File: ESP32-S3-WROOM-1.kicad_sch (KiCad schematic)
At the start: 24 parts, among them J11 Conn_01x08, J13 Conn_02x09_Top_Bottom, J14 Conn_01x09, J15 Conn_02x09_Top_Bottom, J4 B4B-ZRLFSN, J6 Conn_01x09, J7 Conn_02x20_Counter_Clockwise, J8 Conn_01x08, J9 Conn_01x08, SW4 SW_Push, U8 ESP32-S3-WROOM-1-N8R2

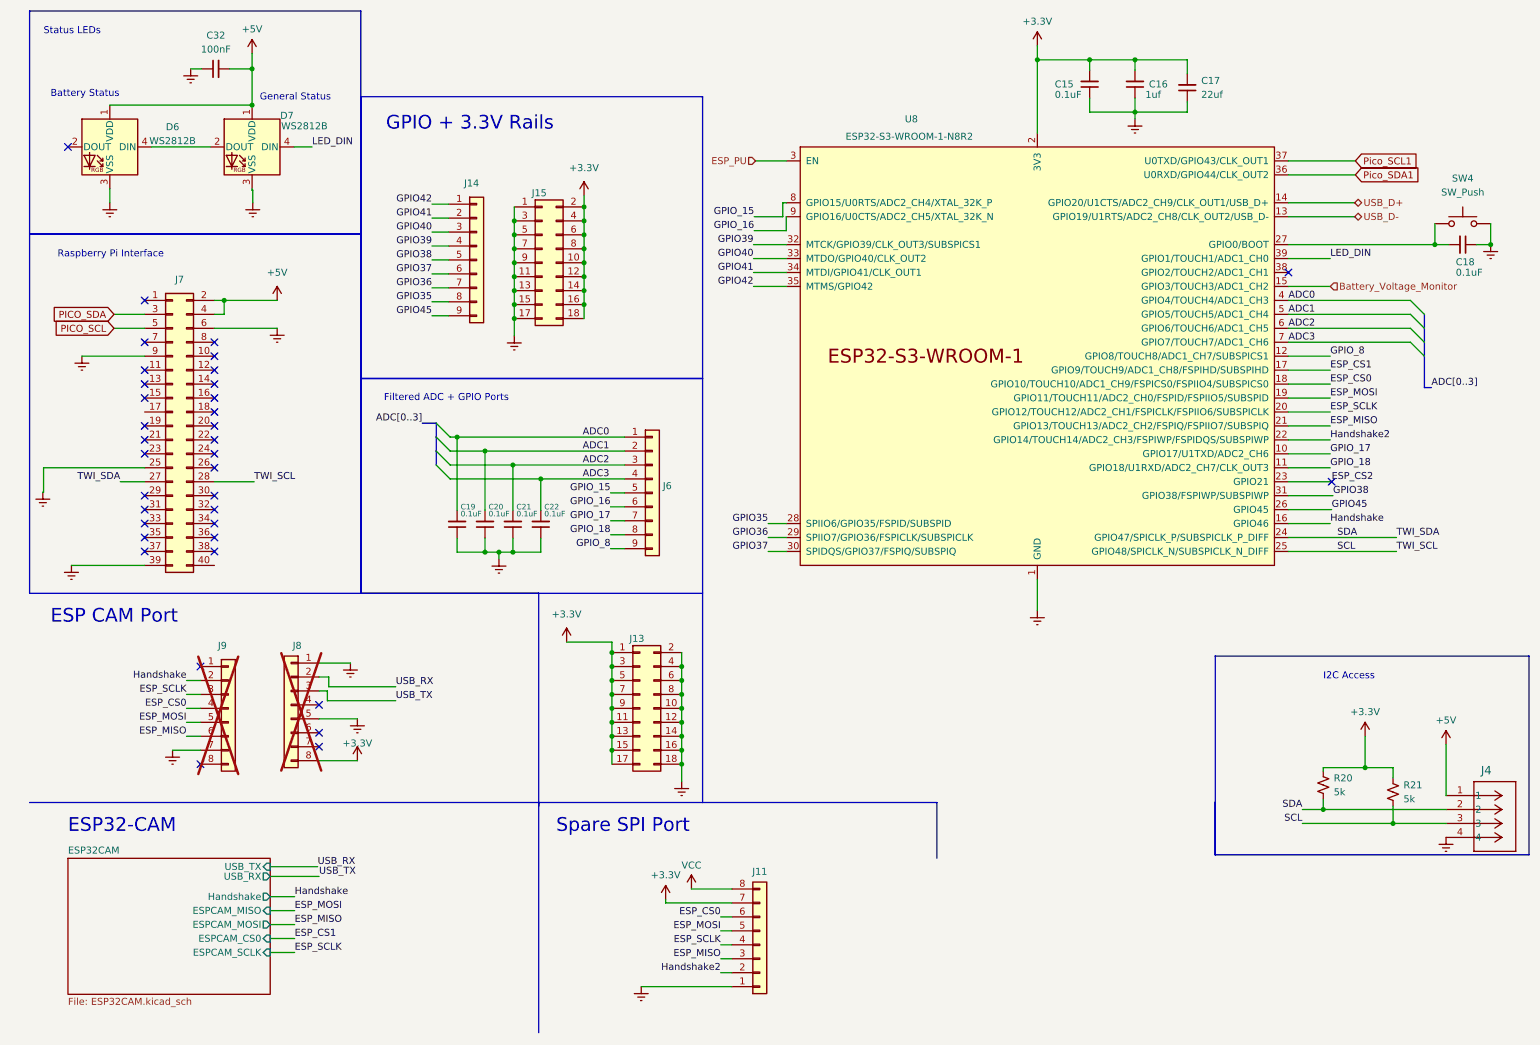
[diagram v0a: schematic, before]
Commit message: Removed 201-sized parts
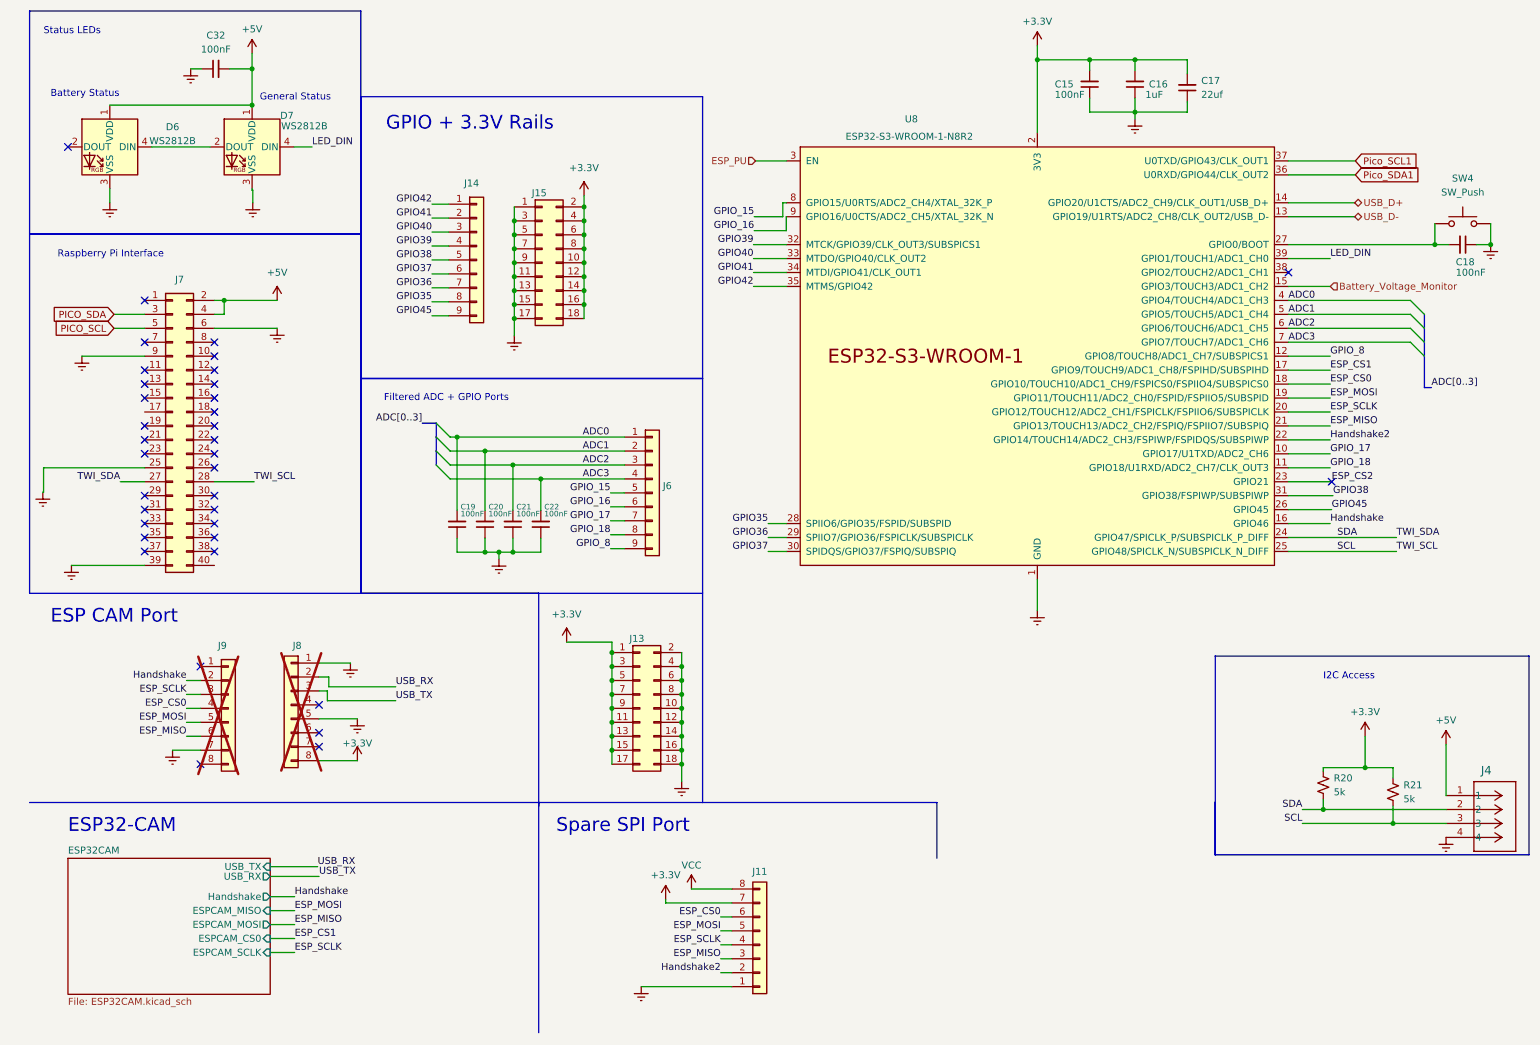
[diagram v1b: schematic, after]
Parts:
- C15, C18, C19, C20, C21, C22: value 0.1uF -> 100nF; LCSC Part # (none) -> C77020
- C16: value 1uf -> 1uF; LCSC Part # (none) -> C14445
- C17: footprint Capacitor_SMD:C_0402_1005Metric -> Capacitor_SMD:C_0603_1608Metric; LCSC Part # (none) -> C86295
- C32: LCSC Part # (none) -> C77020
- D6, D7: LCSC Part # (none) -> C114586
- R20, R21: LCSC Part # (none) -> C5948099
- SW4: LCSC Part # (none) -> C116501
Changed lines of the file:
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@@
       (effects (font (size 1 1)) (justify right))
     )
-    (property "Value" "0.1uF" (at 105.537 103.378 0)
+    (property "Value" "100nF" (at 105.537 103.378 0)
       (effects (font (size 1 1)) (justify right))
     )
@@
       (effects (font (size 1.27 1.27)) hide)
     )
+    (property "LCSC Part #" "C77020" (at 104.902 105.283 0)
+      (effects (font (size 1.27 1.27)) hide)
+    )
     (pin "1")
     (pin "2")
@@
     )
     (property "Datasheet" "~" (at 45.72 22.352 0)
+      (effects (font (size 1.27 1.27)) hide)
+    )
+    (property "LCSC Part #" "C77020" (at 45.72 22.352 0)
       (effects (font (size 1.27 1.27)) hide)
     )
@@
       (effects (font (size 1.27 1.27)) hide)
     )
+    (property "LCSC Part #" "C5948099" (at 247.396 152.781 0)
+      (effects (font (size 1.27 1.27)) hide)
+    )
     (pin "2")
     (pin "1")
@@
     (property "Datasheet" "https://cdn-shop.adafruit.com/datasheets/WS2812B.pdf" (at 49.784 46.101 0)
       (effects (font (size 1.27 1.27)) (justify left top) hide)
+    )
+    (property "LCSC Part #" "C114586" (at 52.324 36.576 0)
+      (effects (font (size 1.27 1.27)) hide)
     )
     (pin "2")
@@
       (effects (font (size 1.27 1.27)) (justify left))
     )
-    (property "Value" "0.1uF" (at 271.526 59.436 90)
+    (property "Value" "100nF" (at 271.526 59.436 90)
       (effects (font (size 1.27 1.27)) (justify left))
     )
@@
     )
     (property "Datasheet" "~" (at 272.796 54.356 0)
+      (effects (font (size 1.27 1.27)) hide)
+    )
+    (property "LCSC Part #" "C77020" (at 272.796 54.356 0)
       (effects (font (size 1.27 1.27)) hide)
     )
@@
       (effects (font (size 1.27 1.27)) (justify right))
     )
-    (property "Footprint" "Capacitor_SMD:C_0402_1005Metric" (at 222.631 25.781 0)
+    (property "Footprint" "Capacitor_SMD:C_0603_1608Metric" (at 222.631 25.781 0)
       (effects (font (size 1.27 1.27)) hide)
     )
     (property "Datasheet" "~" (at 222.631 25.781 0)
+      (effects (font (size 1.27 1.27)) hide)
+    )
+    (property "LCSC Part #" "C86295" (at 222.631 25.781 0)
       (effects (font (size 1.27 1.27)) hide)
     )
@@
       (effects (font (size 1.27 1.27)) hide)
     )
+    (property "LCSC Part #" "C5948099" (at 260.096 154.051 0)
+      (effects (font (size 1.27 1.27)) hide)
+    )
     (pin "2")
     (pin "1")
@@
       (effects (font (size 1 1)) (justify right))
     )
-    (property "Value" "0.1uF" (at 90.297 103.378 0)
+    (property "Value" "100nF" (at 90.297 103.378 0)
       (effects (font (size 1 1)) (justify right))
     )
@@
     )
     (property "Datasheet" "~" (at 89.662 105.283 0)
+      (effects (font (size 1.27 1.27)) hide)
+    )
+    (property "LCSC Part #" "C77020" (at 89.662 105.283 0)
       (effects (font (size 1.27 1.27)) hide)
     )
@@
       (effects (font (size 1 1)) (justify right))
     )
-    (property "Value" "0.1uF" (at 100.457 103.378 0)
+    (property "Value" "100nF" (at 100.457 103.378 0)
       (effects (font (size 1 1)) (justify right))
     )
@@
     )
     (property "Datasheet" "~" (at 99.822 105.283 0)
+      (effects (font (size 1.27 1.27)) hide)
+    )
+    (property "LCSC Part #" "C77020" (at 99.822 105.283 0)
       (effects (font (size 1.27 1.27)) hide)
     )
@@
       (effects (font (size 1.27 1.27)) (justify right))
     )
-    (property "Value" "1uf" (at 215.011 27.051 0)
+    (property "Value" "1uF" (at 215.011 27.051 0)
       (effects (font (size 1.27 1.27)) (justify right))
     )
@@
       (effects (font (size 1.27 1.27)) hide)
     )
+    (property "LCSC Part #" "C14445" (at 213.106 25.146 0)
+      (effects (font (size 1.27 1.27)) hide)
+    )
     (pin "1")
     (pin "2")
@@
     )
     (property "Datasheet" "~" (at 272.796 45.466 0)
+      (effects (font (size 1.27 1.27)) hide)
+    )
+    (property "LCSC Part #" "C116501" (at 272.796 50.546 0)
       (effects (font (size 1.27 1.27)) hide)
     )
@@
       (effects (font (size 1 1)) (justify right))
     )
-    (property "Value" "0.1uF" (at 95.377 103.378 0)
+    (property "Value" "100nF" (at 95.377 103.378 0)
       (effects (font (size 1 1)) (justify right))
     )
@@
     )
     (property "Datasheet" "~" (at 94.742 105.283 0)
+      (effects (font (size 1.27 1.27)) hide)
+    )
+    (property "LCSC Part #" "C77020" (at 94.742 105.283 0)
       (effects (font (size 1.27 1.27)) hide)
     )
@@
     (property "Datasheet" "https://cdn-shop.adafruit.com/datasheets/WS2812B.pdf" (at 23.876 46.101 0)
       (effects (font (size 1.27 1.27)) (justify left top) hide)
+    )
+    (property "LCSC Part #" "C114586" (at 26.416 36.576 0)
+      (effects (font (size 1.27 1.27)) hide)
     )
     (pin "2")
@@
       (effects (font (size 1.27 1.27)) (justify right))
     )
-    (property "Value" "0.1uF" (at 198.501 27.051 0)
+    (property "Value" "100nF" (at 198.501 27.051 0)
       (effects (font (size 1.27 1.27)) (justify right))
     )
@@
       (effects (font (size 1.27 1.27)) hide)
     )
+    (property "LCSC Part #" "C77020" (at 204.851 25.146 0)
+      (effects (font (size 1.27 1.27)) hide)
+    )

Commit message: For production
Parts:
- C15, C18, C19, C20, C21, C22, C32: LCSC Part # C77020 -> C1525
- C16: LCSC Part # C14445 -> C52923
- C17: value 22uf -> 22uF; LCSC Part # C86295 -> C59461
- R20, R21: value 5k -> 5K; LCSC Part # C5948099 -> C25905
- U8: LCSC Part # (none) -> C2913204

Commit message: JLCniceness
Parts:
- J4: value B4B-ZRLFSN -> JST-XH; footprint JST-ZR-4Pin:CONN_B4B-ZRLFSN_JST -> Connector_JST:JST_XH_B4B-XH-AM_1x04_P2.50mm_Vertical
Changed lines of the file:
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@@
 			)
 		)
-		(property "Value" "B4B-ZRLFSN"
+		(property "Value" "JST-XH"
 			(at 283.21 159.766 0)
 			(effects
@@
 			)
 		)
-		(property "Footprint" "JST-ZR-4Pin:CONN_B4B-ZRLFSN_JST"
+		(property "Footprint" "Connector_JST:JST_XH_B4B-XH-AM_1x04_P2.50mm_Vertical"
 			(at 269.748 154.686 0)
 			(effects
@@
 			)
 		)
-		(property "Datasheet" "B4B-ZRLFSN"
+		(property "Datasheet" ""
 			(at 269.748 154.686 0)
 			(effects
@@
 			(at 269.748 154.686 0)
 			(effects
-				(font
-					(size 1.27 1.27)
-				)
-				(hide yes)
-			)
-		)
-		(property "JLCPCB Position Offset" ""
-			(at 269.748 154.686 0)
-			(effects

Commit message: JLC fixes
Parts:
- J4: footprint Connector_JST:JST_XH_B4B-XH-AM_1x04_P2.50mm_Vertical -> Connector_JST:JST_XH_B4B-XH-A_1x04_P2.50mm_Vertical
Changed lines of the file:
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@@
 			)
 		)
-		(property "Footprint" "Connector_JST:JST_XH_B4B-XH-AM_1x04_P2.50mm_Vertical"
+		(property "Footprint" "Connector_JST:JST_XH_B4B-XH-A_1x04_P2.50mm_Vertical"
 			(at 269.748 154.686 0)
 			(effects
@@
 			(effects
 				(font
+					(size 1.27 1.27)
+				)
+				(hide yes)
+			)
+		)
+		(property "LCSC Part # " ""
+			(at 0 309.372 0)
+			(effects
+				(font

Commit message: Rev 2 PCB
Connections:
- net VCC is gone; now on net +5V: J11.8 (Pin_8)
- no-connect marks 36 -> 37
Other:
- moved on the sheet: C15, C16, C17, C19, C20, C21, C22, C32, J14, J15, J4, J6

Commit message: Rev 2 finished
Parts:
- C15, C18, C19, C20, C21, C22, C32: LCSC Part # C1525 -> C307331
- U8: footprint Espressif:ESP32-S3-WROOM-1 -> PCM_Espressif:ESP32-S3-WROOM-1
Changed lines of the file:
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@@
 			)
 		)
-		(property "LCSC Part #" "C1525"
+		(property "LCSC Part #" "C307331"
 			(at 105.41 105.41 0)
 			(effects
@@
 			)
 		)
-		(property "LCSC Part #" "C1525"
+		(property "LCSC Part #" "C307331"
 			(at 45.72 22.86 0)
 			(effects
@@
 			)
 		)
-		(property "LCSC Part #" "C1525"
+		(property "LCSC Part #" "C307331"
 			(at 273.05 54.61 0)
 			(effects
@@
 			)
 		)
-		(property "LCSC Part #" "C1525"
+		(property "LCSC Part #" "C307331"
 			(at 90.17 105.41 0)
 			(effects
@@
 			)
 		)
-		(property "LCSC Part #" "C1525"
+		(property "LCSC Part #" "C307331"
 			(at 100.33 105.41 0)
 			(effects
@@
 			)
 		)
-		(property "Footprint" "Espressif:ESP32-S3-WROOM-1"
+		(property "Footprint" "PCM_Espressif:ESP32-S3-WROOM-1"
 			(at 198.12 123.19 0)
 			(effects
@@
 			)
 		)
-		(property "LCSC Part #" "C1525"
+		(property "LCSC Part #" "C307331"
 			(at 95.25 105.41 0)
 			(effects
@@
 			)
 		)
-		(property "LCSC Part #" "C1525"
+		(property "LCSC Part #" "C307331"
 			(at 204.47 26.67 0)
 			(effects
